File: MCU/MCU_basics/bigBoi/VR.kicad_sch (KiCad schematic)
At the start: 3 parts, among them U2 LT1963AxST-3.3

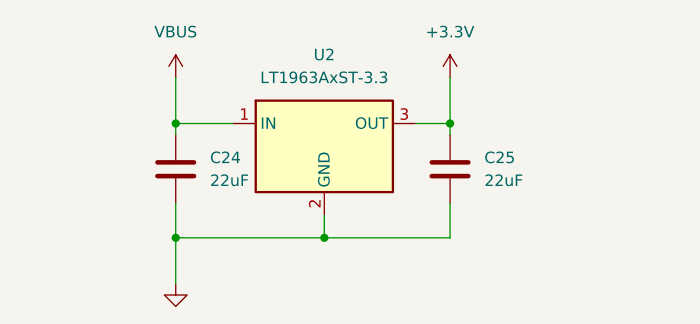
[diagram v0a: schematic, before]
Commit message: schematic connections
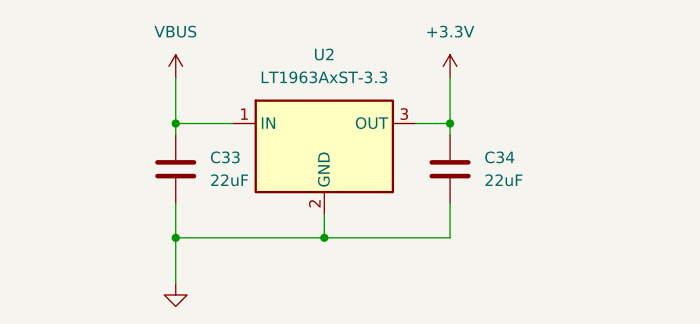
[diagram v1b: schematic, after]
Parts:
- renumbered C24 to C33, C25 to C34
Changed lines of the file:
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@@
 		(dnp no)
 		(fields_autoplaced yes)
-		(property "Reference" "#PWR014"
+		(property "Reference" "#PWR026"
 			(at 66.04 36.83 0)
 			(hide yes)
@@
 			(project "bigBoi"
 				(path "/0a118c22-2522-42a6-b7a6-70c79326ece4/db613e93-62d9-4c37-b5dd-6dfd220d38f7"
-					(reference "#PWR014")
+					(reference "#PWR026")
 					(unit 1)
 				)
@@
 		(dnp no)
 		(fields_autoplaced yes)
-		(property "Reference" "C24"
+		(property "Reference" "C33"
 			(at 39.37 41.9099 0)
 			(show_name no)
@@
 			(project "bigBoi"
 				(path "/0a118c22-2522-42a6-b7a6-70c79326ece4/db613e93-62d9-4c37-b5dd-6dfd220d38f7"
-					(reference "C24")
+					(reference "C33")
 					(unit 1)
 				)
@@
 		(dnp no)
 		(fields_autoplaced yes)
-		(property "Reference" "#PWR012"
+		(property "Reference" "#PWR024"
 			(at 35.56 36.83 0)
 			(hide yes)
@@
 			(project "bigBoi"
 				(path "/0a118c22-2522-42a6-b7a6-70c79326ece4/db613e93-62d9-4c37-b5dd-6dfd220d38f7"
-					(reference "#PWR012")
+					(reference "#PWR024")
 					(unit 1)
 				)
@@
 		(dnp no)
 		(fields_autoplaced yes)
-		(property "Reference" "C25"
+		(property "Reference" "C34"
 			(at 69.85 41.9099 0)
 			(show_name no)
@@
 			(project "bigBoi"
 				(path "/0a118c22-2522-42a6-b7a6-70c79326ece4/db613e93-62d9-4c37-b5dd-6dfd220d38f7"
-					(reference "C25")
+					(reference "C34")
 					(unit 1)
 				)
@@
 		(dnp no)
 		(fields_autoplaced yes)
-		(property "Reference" "#PWR013"
+		(property "Reference" "#PWR025"
 			(at 35.56 62.23 0)
 			(hide yes)
@@
 			(project "bigBoi"
 				(path "/0a118c22-2522-42a6-b7a6-70c79326ece4/db613e93-62d9-4c37-b5dd-6dfd220d38f7"
-					(reference "#PWR013")
-					(unit 1)
-				)
+					(reference "#PWR025")
+					(unit 1)
+				)

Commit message: ERC resolving
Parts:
- added D2: GREEN, LED_SMD:LED_0603_1608Metric, symbol Device:LED
- added R7: 1k5, Resistor_SMD:R_0402_1005Metric, symbol Device:R
- C33, C34: footprint (none) -> Capacitor_SMD:C_0805_2012Metric
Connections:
- net +3.3V: now also D2.2 (A)
- net GND: now also R7.2
- new net: D2.1 (K), R7.1
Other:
- note added: "power on light"
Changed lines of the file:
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@@
 	(generator_version "10.0")
 	(paper "A4")
+	(text "power on light"
+		(exclude_from_sim no)
+		(at 80.264 27.94 0)
+		(effects
+			(font
+				(size 1.27 1.27)
+			)
+		)
+	)
 	(junction
 		(at 66.04 38.1)
@@
 	)
 	(junction
+		(at 66.04 50.8)
+		(diameter 0)
+		(color 0 0 0 0)
+	)
+	(junction
 		(at 52.07 50.8)
 		(diameter 0)
@@
 	(wire
 		(pts
+			(xy 85.09 50.8) (xy 66.04 50.8)
+		)
+		(stroke
+			(width 0)
+			(type default)
+		)
+	)
+	(wire
+		(pts
+			(xy 85.09 48.26) (xy 85.09 50.8)
+		)
+		(stroke
+			(width 0)
+			(type default)
+		)
+	)
+	(wire
+		(pts
 			(xy 52.07 50.8) (xy 66.04 50.8)
 		)
@@
 	(wire
 		(pts
+			(xy 85.09 38.1) (xy 85.09 40.64)
+		)
+		(stroke
+			(width 0)
+			(type default)
+		)
+	)
+	(wire
+		(pts
 			(xy 35.56 38.1) (xy 41.91 38.1)
 		)
@@
 	(wire
 		(pts
+			(xy 66.04 38.1) (xy 74.93 38.1)
+		)
+		(stroke
+			(width 0)
+			(type default)
+		)
+	)
+	(wire
+		(pts
+			(xy 82.55 38.1) (xy 85.09 38.1)
+		)
+		(stroke
+			(width 0)
+			(type default)
+		)
+	)
+	(wire
+		(pts
 			(xy 66.04 46.99) (xy 66.04 50.8)
 		)
@@
 			(width 0)
 			(type default)
+		)
+	)
+	(symbol
+		(lib_id "Device:R")
+		(at 85.09 44.45 0)
+		(unit 1)
+		(body_style 1)
+		(exclude_from_sim no)
+		(in_bom yes)
+		(on_board yes)
+		(in_pos_files yes)
+		(dnp no)
+		(fields_autoplaced yes)
+		(property "Reference" "R7"
+			(at 87.63 43.1799 0)
+			(show_name no)
+			(do_not_autoplace no)
+			(effects
+				(font
+					(size 1.27 1.27)
+				)
+				(justify left)
+			)
+		)
+		(property "Value" "1k5"
+			(at 87.63 45.7199 0)
+			(show_name no)
+			(do_not_autoplace no)
+			(effects
+				(font
+					(size 1.27 1.27)
+				)
+				(justify left)
+			)
+		)
+		(property "Footprint" "Resistor_SMD:R_0402_1005Metric"
+			(at 83.312 44.45 90)
+			(hide yes)
+			(show_name no)
+			(do_not_autoplace no)
+			(effects
+				(font
+					(size 1.27 1.27)
+				)
+			)
+		)
+		(property "Datasheet" ""
+			(at 85.09 44.45 0)
+			(hide yes)
+			(show_name no)
+			(do_not_autoplace no)
+			(effects
+				(font
+					(size 1.27 1.27)
+				)
+			)
+		)
+		(property "Description" "Resistor"
+			(at 85.09 44.45 0)
+			(hide yes)
+			(show_name no)
+			(do_not_autoplace no)
+			(effects
+				(font
+					(size 1.27 1.27)
+				)
+			)
+		)
+		(pin "1"
+		)
+		(pin "2"
+		)
+		(instances
+			(project "bigBoi"
+				(path "/0a118c22-2522-42a6-b7a6-70c79326ece4/db613e93-62d9-4c37-b5dd-6dfd220d38f7"
+					(reference "R7")
+					(unit 1)
+				)
+			)
 		)
 	)
@@
 			)
 		)
-		(property "Footprint" ""
+		(property "Footprint" "Capacitor_SMD:C_0805_2012Metric"
 			(at 36.5252 46.99 0)
 			(hide yes)
@@
 	)
 	(symbol
+		(lib_id "Device:LED")
+		(at 78.74 38.1 180)
+		(unit 1)
+		(body_style 1)
+		(exclude_from_sim no)
+		(in_bom yes)
+		(on_board yes)
+		(in_pos_files yes)
+		(dnp no)
+		(fields_autoplaced yes)
+		(property "Reference" "D2"
+			(at 80.3275 30.48 0)
+			(show_name no)
+			(do_not_autoplace no)
+			(effects
+				(font
+					(size 1.27 1.27)
+				)
+			)
+		)
+		(property "Value" "GREEN"
+			(at 80.3275 33.02 0)
+			(show_name no)
+			(do_not_autoplace no)
+			(effects
+				(font
+					(size 1.27 1.27)
+				)
+			)
+		)
+		(property "Footprint" "LED_SMD:LED_0603_1608Metric"
+			(at 78.74 38.1 0)
+			(hide yes)
+			(show_name no)
+			(do_not_autoplace no)
+			(effects
+				(font
+					(size 1.27 1.27)
+				)
+			)
+		)
+		(property "Datasheet" ""
+			(at 78.74 38.1 0)
+			(hide yes)
+			(show_name no)
+			(do_not_autoplace no)
+			(effects
+				(font
+					(size 1.27 1.27)
+				)
+			)
+		)
+		(property "Description" "Light emitting diode"
+			(at 78.74 38.1 0)
+			(hide yes)
+			(show_name no)
+			(do_not_autoplace no)
+			(effects
+				(font
+					(size 1.27 1.27)
+				)
+			)
+		)
+		(property "Sim.Pins" "1=K 2=A"
+			(at 78.74 38.1 0)
+			(hide yes)
+			(show_name no)
+			(do_not_autoplace no)
+			(effects
+				(font
+					(size 1.27 1.27)
+				)
+			)
+		)
+		(pin "1"
+		)
+		(pin "2"
+		)
+		(instances
+			(project "bigBoi"
+				(path "/0a118c22-2522-42a6-b7a6-70c79326ece4/db613e93-62d9-4c37-b5dd-6dfd220d38f7"
+					(reference "D2")
+					(unit 1)
+				)
+			)
+		)
+	)
+	(symbol
 		(lib_id "power:VBUS")
 		(at 35.56 33.02 0)
@@
 			)
 		)
-		(property "Footprint" ""
+		(property "Footprint" "Capacitor_SMD:C_0805_2012Metric"
 			(at 67.0052 46.99 0)
 			(hide yes)

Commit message: Bat
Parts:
- added BT1: Battery, Connector_JST:JST_PH_S2B-PH-K_1x02_P2.00mm_Horizontal, symbol Device:Battery
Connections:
- net GND: now also BT1.2 (-)
- net VBUS: now also BT1.1 (+)
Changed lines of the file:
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@@
+	)
+	(junction
+		(at 35.56 35.56)
+		(diameter 0)
+		(color 0 0 0 0)
 	)
 	(junction
@@
 	(wire
 		(pts
-			(xy 35.56 33.02) (xy 35.56 38.1)
+			(xy 35.56 33.02) (xy 35.56 35.56)
+		)
+		(stroke
+			(width 0)
+			(type default)
+		)
+	)
+	(wire
+		(pts
+			(xy 20.32 35.56) (xy 35.56 35.56)
+		)
+		(stroke
+			(width 0)
+			(type default)
+		)
+	)
+	(wire
+		(pts
+			(xy 35.56 35.56) (xy 35.56 38.1)
 		)
 		(stroke
@@
 		(pts
 			(xy 35.56 38.1) (xy 35.56 39.37)
+		)
+		(stroke
+			(width 0)
+			(type default)
+		)
+	)
+	(wire
+		(pts
+			(xy 20.32 36.83) (xy 20.32 35.56)
 		)
 		(stroke
@@
 	)
 	(symbol
+		(lib_id "power:GND")
+		(at 20.32 46.99 0)
+		(unit 1)
+		(body_style 1)
+		(exclude_from_sim no)
+		(in_bom yes)
+		(on_board yes)
+		(in_pos_files yes)
+		(dnp no)
+		(fields_autoplaced yes)
+		(property "Reference" "#PWR077"
+			(at 20.32 53.34 0)
+			(hide yes)
+			(show_name no)
+			(do_not_autoplace no)
+			(effects
+				(font
+					(size 1.27 1.27)
+				)
+			)
+		)
+		(property "Value" "GND"
+			(at 20.32 52.07 0)
+			(hide yes)
+			(show_name no)
+			(do_not_autoplace no)
+			(effects
+				(font
+					(size 1.27 1.27)
+				)
+			)
+		)
+		(property "Footprint" ""
+			(at 20.32 46.99 0)
+			(hide yes)
+			(show_name no)
+			(do_not_autoplace no)
+			(effects
+				(font
+					(size 1.27 1.27)
+				)
+			)
+		)
+		(property "Datasheet" ""
+			(at 20.32 46.99 0)
+			(hide yes)
+			(show_name no)
+			(do_not_autoplace no)
+			(effects
+				(font
+					(size 1.27 1.27)
+				)
+			)
+		)
+		(property "Description" "Power symbol creates a global label with name \"GND\" , ground"
+			(at 20.32 46.99 0)
+			(hide yes)
+			(show_name no)
+			(do_not_autoplace no)
+			(effects
+				(font
+					(size 1.27 1.27)
+				)
+			)
+		)
+		(pin "1"
+		)
+		(instances
+			(project "bigBoi"
+				(path "/0a118c22-2522-42a6-b7a6-70c79326ece4/db613e93-62d9-4c37-b5dd-6dfd220d38f7"
+					(reference "#PWR077")
+					(unit 1)
+				)
+			)
+		)
+	)
+	(symbol
 		(lib_id "Device:C")
 		(at 35.56 43.18 0)
@@
 					(unit 1)
 				)
+			)
+		)
+	)
+	(symbol
+		(lib_id "Device:Battery")
+		(at 20.32 41.91 0)
+		(unit 1)
+		(body_style 1)
+		(exclude_from_sim no)
+		(in_bom yes)
+		(on_board yes)
+		(in_pos_files yes)
+		(dnp no)
+		(fields_autoplaced yes)
+		(property "Reference" "BT1"
+			(at 24.13 40.0684 0)
+			(show_name no)
+			(do_not_autoplace no)
+			(effects
+				(font
+					(size 1.27 1.27)
+				)
+				(justify left)
+			)
+		)
+		(property "Value" "Battery"
+			(at 24.13 42.6084 0)
+			(show_name no)
+			(do_not_autoplace no)
+			(effects
+				(font
+					(size 1.27 1.27)
+				)
+				(justify left)
+			)
+		)
+		(property "Footprint" "Connector_JST:JST_PH_S2B-PH-K_1x02_P2.00mm_Horizontal"
+			(at 20.32 40.386 90)
+			(hide yes)
+			(show_name no)
+			(do_not_autoplace no)
+			(effects
+				(font
+					(size 1.27 1.27)
+				)
+			)
+		)
+		(property "Datasheet" ""
+			(at 20.32 40.386 90)
+			(hide yes)
+			(show_name no)
+			(do_not_autoplace no)
+			(effects
+				(font
+					(size 1.27 1.27)
+				)
+			)
+		)
+		(property "Description" "Multiple-cell battery"
+			(at 20.32 41.91 0)
+			(hide yes)
+			(show_name no)
+			(do_not_autoplace no)
+			(effects
+				(font
+					(size 1.27 1.27)
+				)
+			)
+		)
+		(property "Sim.Device" "V"
+			(at 20.32 41.91 0)
+			(hide yes)
+			(show_name no)
+			(do_not_autoplace no)
+			(effects
+				(font
+					(size 1.27 1.27)
+				)
+			)
+		)
+		(property "Sim.Type" "DC"
+			(at 20.32 41.91 0)
+			(hide yes)
+			(show_name no)
+			(do_not_autoplace no)
+			(effects
+				(font
+					(size 1.27 1.27)
+				)
+			)
+		)
+		(property "Sim.Pins" "1=+ 2=-"
+			(at 20.32 41.91 0)
+			(hide yes)
+			(show_name no)
+			(do_not_autoplace no)
+			(effects
+				(font
+					(size 1.27 1.27)
+				)
+			)
+		)
+		(pin "2"
+		)
+		(pin "1"
+		)
+		(instances
+			(project "bigBoi"
+				(path "/0a118c22-2522-42a6-b7a6-70c79326ece4/db613e93-62d9-4c37-b5dd-6dfd220d38f7"
+					(reference "BT1")
+					(unit 1)
+				)
